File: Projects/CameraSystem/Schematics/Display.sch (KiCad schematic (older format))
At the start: 7 parts, among them U8 PCA9306D_118, U9 LCD_2x16_w_i2c

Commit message: feat: assign footprints
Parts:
- U9: footprint (none) -> Pin_Headers:Pin_Header_Straight_1x04_Pitch2.54mm
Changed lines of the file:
@@
 $Descr A4 11693 8268
 encoding utf-8
-Sheet 7 9
+Sheet 6 9
 Title ""
 Date ""
@@
 F 0 "U9" H 6350 1950 60  0000 C CNN
 F 1 "LCD_2x16_w_i2c" H 6350 2650 60  0000 C CNN
-F 2 "" H 6350 2300 60  0001 C CNN
+F 2 "Pin_Headers:Pin_Header_Straight_1x04_Pitch2.54mm" H 6350 2300 60  0001 C CNN
 F 3 "" H 6350 2300 60  0001 C CNN
 	1    6350 2300

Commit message: linux adaptation
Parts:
- added R?: 200k, digikey-footprints:0603, symbol Device:R
- U9: symbol cl-integrated_circuits:LCD_2x16_w_i2c -> CameraSystem-rescue:LCD_2x16_w_i2c-cl-integrated_circuits
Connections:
- wire segments 34 -> 35
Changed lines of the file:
@@
 SCL_3V3
 $Comp
-L cl-integrated_circuits:LCD_2x16_w_i2c U9
+L CameraSystem-rescue:LCD_2x16_w_i2c-cl-integrated_circuits U9
 U 1 1 5BB9D5E3
 P 6350 2300
+AR Path="/5BB9D5E3" Ref="U9"  Part="1"
+AR Path="/5BB9CC6E/5BB9D5E3" Ref="U9"  Part="1"
 F 0 "U9" H 6350 1950 60  0000 C CNN
 F 1 "LCD_2x16_w_i2c" H 6350 2650 60  0000 C CNN
@@
 	1    0    0    -1
 $EndComp
-Text Label 6700 4150 0    60   ~ 0
+Text Label 7300 4150 0    60   ~ 0
 VDD_5V0
 Wire Wire Line
@@
 Wire Wire Line
 	4300 4850 5700 4850
+$Comp
+L Device:R R?
+U 1 1 5CA52D89
+P 6850 4150
+F 0 "R?" V 6930 4150 50  0000 C CNN
+F 1 "200k" V 6850 4150 50  0000 C CNN
+F 2 "digikey-footprints:0603" V 6780 4150 50  0001 C CNN
+F 3 "" H 6850 4150 50  0001 C CNN
+	1    6850 4150
+	0    1    1    0
+$EndComp
+Wire Wire Line
+	7000 4150 7300 4150
 $EndSCHEMATC

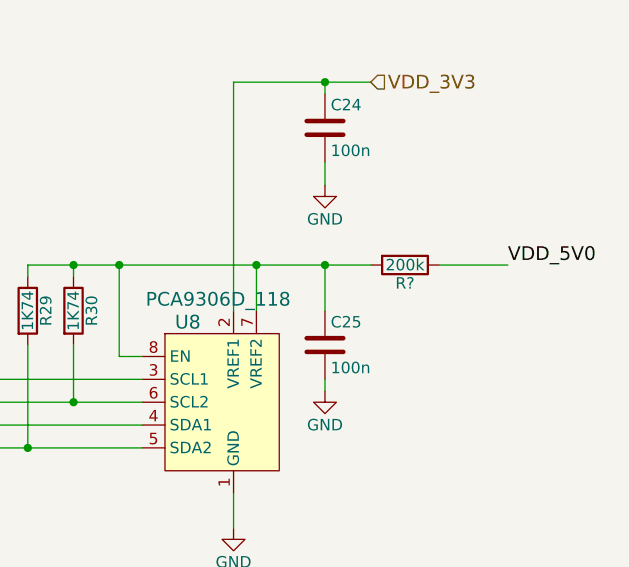
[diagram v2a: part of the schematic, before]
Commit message: wifi module added
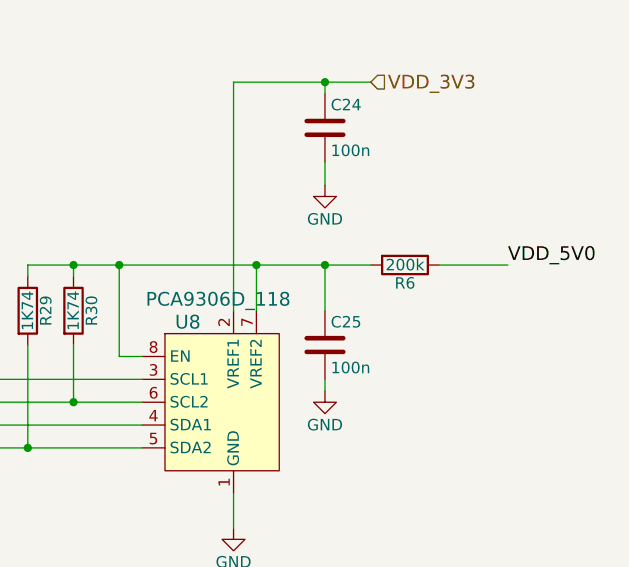
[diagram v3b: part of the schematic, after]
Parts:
- gave numbers to parts that had none: 1
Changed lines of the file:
@@
 	4300 4850 5700 4850
 $Comp
-L Device:R R?
+L Device:R R6
 U 1 1 5CA52D89
 P 6850 4150
-F 0 "R?" V 6930 4150 50  0000 C CNN
+F 0 "R6" V 6930 4150 50  0000 C CNN
 F 1 "200k" V 6850 4150 50  0000 C CNN
 F 2 "digikey-footprints:0603" V 6780 4150 50  0001 C CNN

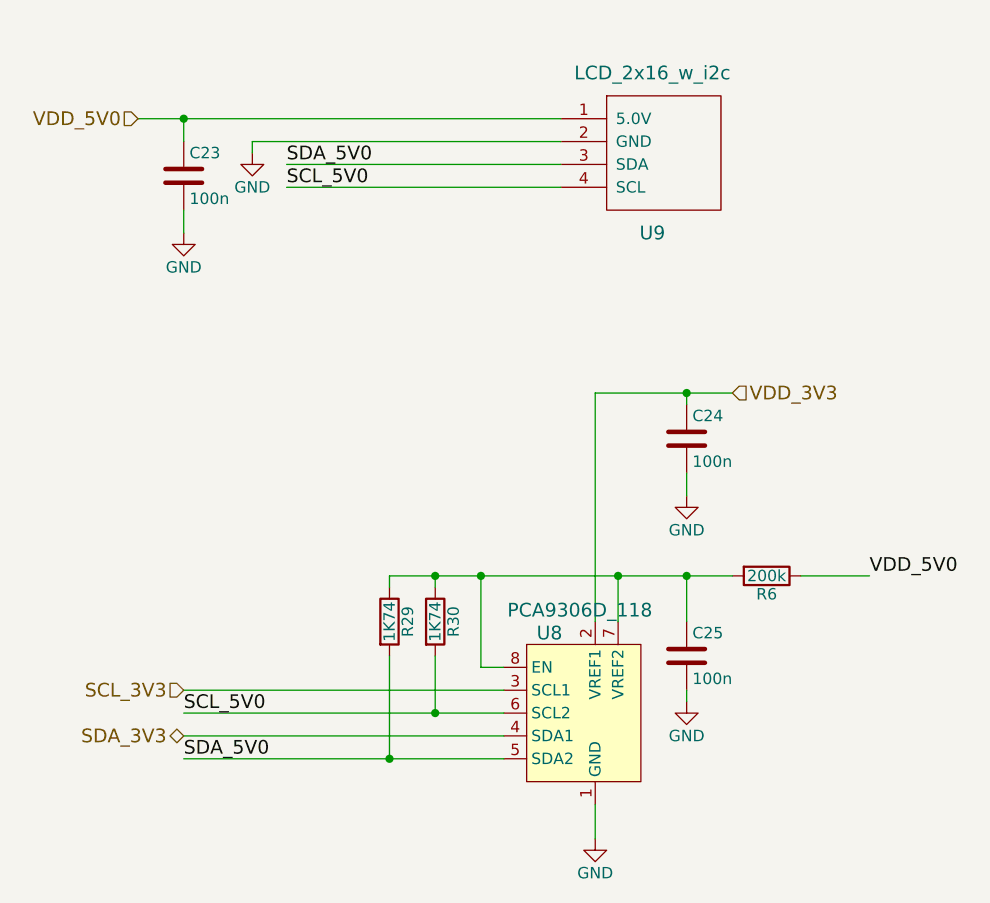
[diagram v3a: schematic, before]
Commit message: camera was updated
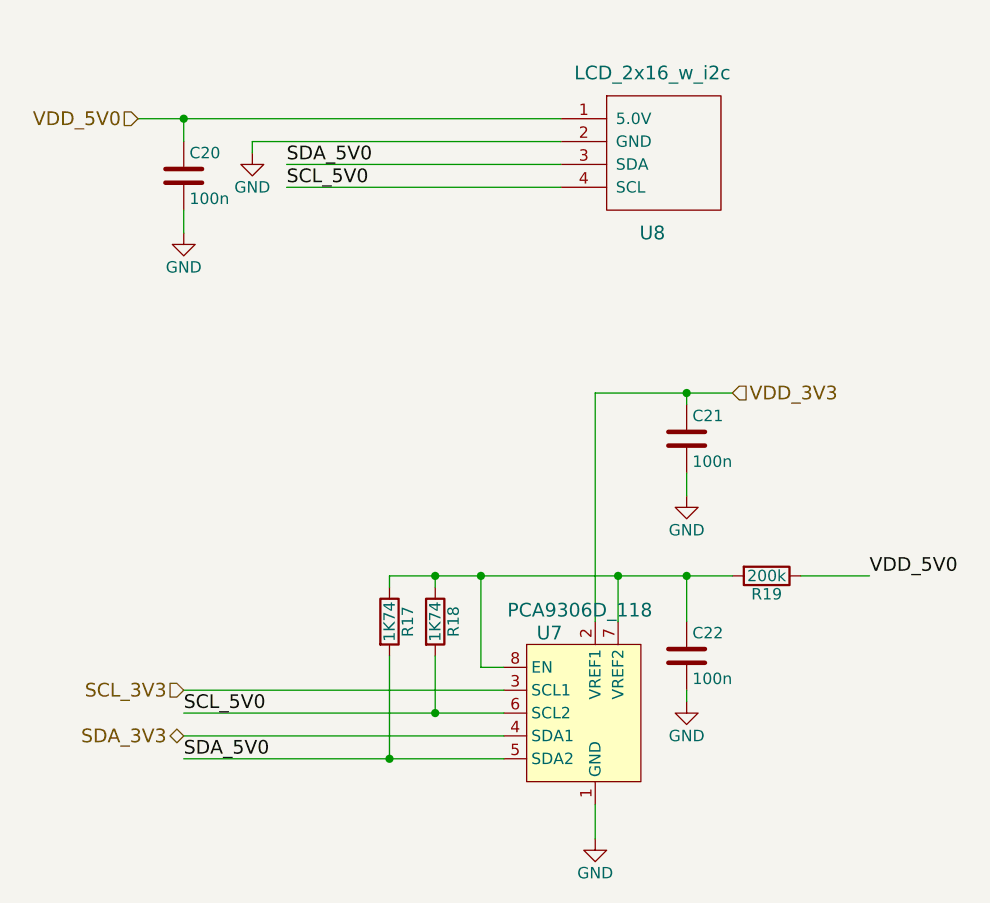
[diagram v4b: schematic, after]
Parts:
- C20: renamed from C23; footprint digikey-footprints:0603 -> Capacitor_SMD:C_0603_1608Metric_Pad1.05x0.95mm_HandSolder
- C21: renamed from C24; footprint digikey-footprints:0603 -> Capacitor_SMD:C_0603_1608Metric_Pad1.05x0.95mm_HandSolder
- C22: renamed from C25; footprint digikey-footprints:0603 -> Capacitor_SMD:C_0603_1608Metric_Pad1.05x0.95mm_HandSolder
- R17: renamed from R29; footprint digikey-footprints:0603 -> Resistor_SMD:R_0603_1608Metric_Pad1.05x0.95mm_HandSolder
- R18: renamed from R30; footprint digikey-footprints:0603 -> Resistor_SMD:R_0603_1608Metric_Pad1.05x0.95mm_HandSolder
- R19: renamed from R6; footprint digikey-footprints:0603 -> Resistor_SMD:R_0603_1608Metric_Pad1.05x0.95mm_HandSolder
- U8: renamed from U9; footprint Pin_Headers:Pin_Header_Straight_1x04_Pitch2.54mm -> Connector_PinSocket_2.54mm:PinSocket_1x04_P2.54mm_Vertical
- renumbered U8 to U7
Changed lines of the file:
@@
 EESchema Schematic File Version 4
 LIBS:CameraSystem-cache
-EELAYER 26 0
+EELAYER 29 0
 EELAYER END
 $Descr A4 11693 8268
@@
 SCL_3V3
 $Comp
-L CameraSystem-rescue:LCD_2x16_w_i2c-cl-integrated_circuits U9
+L CameraSystem-rescue:LCD_2x16_w_i2c-cl-integrated_circuits U?
 U 1 1 5BB9D5E3
 P 6350 2300
-AR Path="/5BB9D5E3" Ref="U9"  Part="1"
-AR Path="/5BB9CC6E/5BB9D5E3" Ref="U9"  Part="1"
-F 0 "U9" H 6350 1950 60  0000 C CNN
+AR Path="/5BB9D5E3" Ref="U?"  Part="1"
+AR Path="/5BB9CC6E/5BB9D5E3" Ref="U8"  Part="1"
+F 0 "U8" H 6350 1950 60  0000 C CNN
 F 1 "LCD_2x16_w_i2c" H 6350 2650 60  0000 C CNN
-F 2 "Pin_Headers:Pin_Header_Straight_1x04_Pitch2.54mm" H 6350 2300 60  0001 C CNN
+F 2 "Connector_PinSocket_2.54mm:PinSocket_1x04_P2.54mm_Vertical" H 6350 2300 60  0001 C CNN
 F 3 "" H 6350 2300 60  0001 C CNN
 	1    6350 2300
@@
 $EndComp
 $Comp
-L power:GND #PWR0136
+L power:GND #PWR031
 U 1 1 5BB9D659
 P 4600 2300
-F 0 "#PWR0136" H 4600 2050 50  0001 C CNN
+F 0 "#PWR031" H 4600 2050 50  0001 C CNN
 F 1 "GND" H 4600 2150 50  0000 C CNN
 F 2 "" H 4600 2300 50  0001 C CNN
@@
 $EndComp
 $Comp
-L Device:C C23
+L Device:C C20
 U 1 1 5BB9D673
 P 4300 2400
-F 0 "C23" H 4325 2500 50  0000 L CNN
+F 0 "C20" H 4325 2500 50  0000 L CNN
 F 1 "100n" H 4325 2300 50  0000 L CNN
-F 2 "digikey-footprints:0603" H 4338 2250 50  0001 C CNN
+F 2 "Capacitor_SMD:C_0603_1608Metric_Pad1.05x0.95mm_HandSolder" H 4338 2250 50  0001 C CNN
 F 3 "" H 4300 2400 50  0001 C CNN
 	1    4300 2400
@@
 Connection ~ 4300 2150
 $Comp
-L power:GND #PWR0137
+L power:GND #PWR030
 U 1 1 5BB9D6EF
 P 4300 2650
-F 0 "#PWR0137" H 4300 2400 50  0001 C CNN
+F 0 "#PWR030" H 4300 2400 50  0001 C CNN
 F 1 "GND" H 4300 2500 50  0000 C CNN
 F 2 "" H 4300 2650 50  0001 C CNN
@@
 P 6100 4850
 AR Path="/5BB9DA52" Ref="U?"  Part="1"
-AR Path="/5BB9CC6E/5BB9DA52" Ref="U8"  Part="1"
-F 0 "U8" H 5900 5300 60  0000 C CNN
+AR Path="/5BB9CC6E/5BB9DA52" Ref="U7"  Part="1"
+F 0 "U7" H 5900 5300 60  0000 C CNN
 F 1 "PCA9306D_118" H 6350 5400 60  0000 R CNN
 F 2 "digikey-footprints:SOIC-8_W3.9mm" H 6300 5050 60  0001 L CNN
@@
 Connection ~ 6200 4150
 $Comp
-L Device:C C25
+L Device:C C22
 U 1 1 5BB9DC5C
 P 6500 4500
-F 0 "C25" H 6525 4600 50  0000 L CNN
+F 0 "C22" H 6525 4600 50  0000 L CNN
 F 1 "100n" H 6525 4400 50  0000 L CNN
-F 2 "digikey-footprints:0603" H 6538 4350 50  0001 C CNN
+F 2 "Capacitor_SMD:C_0603_1608Metric_Pad1.05x0.95mm_HandSolder" H 6538 4350 50  0001 C CNN
 F 3 "" H 6500 4500 50  0001 C CNN
 	1    6500 4500
@@
 	6500 4650 6500 4700
 $Comp
-L power:GND #PWR0138
+L power:GND #PWR034
 U 1 1 5BB9DD24
 P 6500 4700
-F 0 "#PWR0138" H 6500 4450 50  0001 C CNN
+F 0 "#PWR034" H 6500 4450 50  0001 C CNN
 F 1 "GND" H 6500 4550 50  0000 C CNN
 F 2 "" H 6500 4700 50  0001 C CNN
@@
 	6100 3350 6100 4350
 $Comp
-L Device:C C24
+L Device:C C21
 U 1 1 5BB9DEB0
 P 6500 3550
-F 0 "C24" H 6525 3650 50  0000 L CNN
+F 0 "C21" H 6525 3650 50  0000 L CNN
 F 1 "100n" H 6525 3450 50  0000 L CNN
-F 2 "digikey-footprints:0603" H 6538 3400 50  0001 C CNN
+F 2 "Capacitor_SMD:C_0603_1608Metric_Pad1.05x0.95mm_HandSolder" H 6538 3400 50  0001 C CNN
 F 3 "" H 6500 3550 50  0001 C CNN
 	1    6500 3550
@@
 Connection ~ 6500 3350
 $Comp
-L power:GND #PWR0139
+L power:GND #PWR033
 U 1 1 5BB9DF83
 P 6500 3800
-F 0 "#PWR0139" H 6500 3550 50  0001 C CNN
+F 0 "#PWR033" H 6500 3550 50  0001 C CNN
 F 1 "GND" H 6500 3650 50  0000 C CNN
 F 2 "" H 6500 3800 50  0001 C CNN
@@
 	6500 3700 6500 3800
 $Comp
-L power:GND #PWR0140
+L power:GND #PWR032
 U 1 1 5BB9DFE6
 P 6100 5300
-F 0 "#PWR0140" H 6100 5050 50  0001 C CNN
+F 0 "#PWR032" H 6100 5050 50  0001 C CNN
 F 1 "GND" H 6100 5150 50  0000 C CNN
 F 2 "" H 6100 5300 50  0001 C CNN
@@
 	6100 5150 6100 5300
 $Comp
-L Device:R R29
+L Device:R R17
 U 1 1 5BB9E244
 P 5200 4350
-F 0 "R29" V 5280 4350 50  0000 C CNN
+F 0 "R17" V 5280 4350 50  0000 C CNN
 F 1 "1K74" V 5200 4350 50  0000 C CNN
-F 2 "digikey-footprints:0603" V 5130 4350 50  0001 C CNN
+F 2 "Resistor_SMD:R_0603_1608Metric_Pad1.05x0.95mm_HandSolder" V 5130 4350 50  0001 C CNN
 F 3 "" H 5200 4350 50  0001 C CNN
 	1    5200 4350
@@
 SCL_5V0
 $Comp
-L Device:R R30
+L Device:R R18
 U 1 1 5BB9E8B2
 P 5400 4350
-F 0 "R30" V 5480 4350 50  0000 C CNN
+F 0 "R18" V 5480 4350 50  0000 C CNN
 F 1 "1K74" V 5400 4350 50  0000 C CNN
-F 2 "digikey-footprints:0603" V 5330 4350 50  0001 C CNN
+F 2 "Resistor_SMD:R_0603_1608Metric_Pad1.05x0.95mm_HandSolder" V 5330 4350 50  0001 C CNN
 F 3 "" H 5400 4350 50  0001 C CNN
 	1    5400 4350
@@
 	4300 4850 5700 4850
 $Comp
-L Device:R R6
+L Device:R R19
 U 1 1 5CA52D89
 P 6850 4150
-F 0 "R6" V 6930 4150 50  0000 C CNN
+F 0 "R19" V 6930 4150 50  0000 C CNN
 F 1 "200k" V 6850 4150 50  0000 C CNN
-F 2 "digikey-footprints:0603" V 6780 4150 50  0001 C CNN
+F 2 "Resistor_SMD:R_0603_1608Metric_Pad1.05x0.95mm_HandSolder" V 6780 4150 50  0001 C CNN
 F 3 "" H 6850 4150 50  0001 C CNN
 	1    6850 4150
